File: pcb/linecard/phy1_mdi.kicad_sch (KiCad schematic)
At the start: 51 parts, among them J5 LPJT476156AENL, J9 LPJT476156AENL, U35 VSC8512, U36 ESD224DQAR, U37 ESD224DQAR, U38 ESD224DQAR, U39 ESD224DQAR, U40 ESD224DQAR, U41 ESD224DQAR, U42 ESD224DQAR, U43 ESD224DQAR, U44 ESD224DQAR, U45 ESD224DQAR, U46 ESD224DQAR, U47 ESD224DQAR, U48 ESD224DQAR, U49 ESD224DQAR, U50 ESD224DQAR, U51 ESD224DQAR, U52 ESD224DQAR, U53 ESD224DQAR, U54 ESD224DQAR, U55 ESD224DQAR, U56 ESD224DQAR, U57 ESD224DQAR, U58 ESD224DQAR, U59 ESD224DQAR

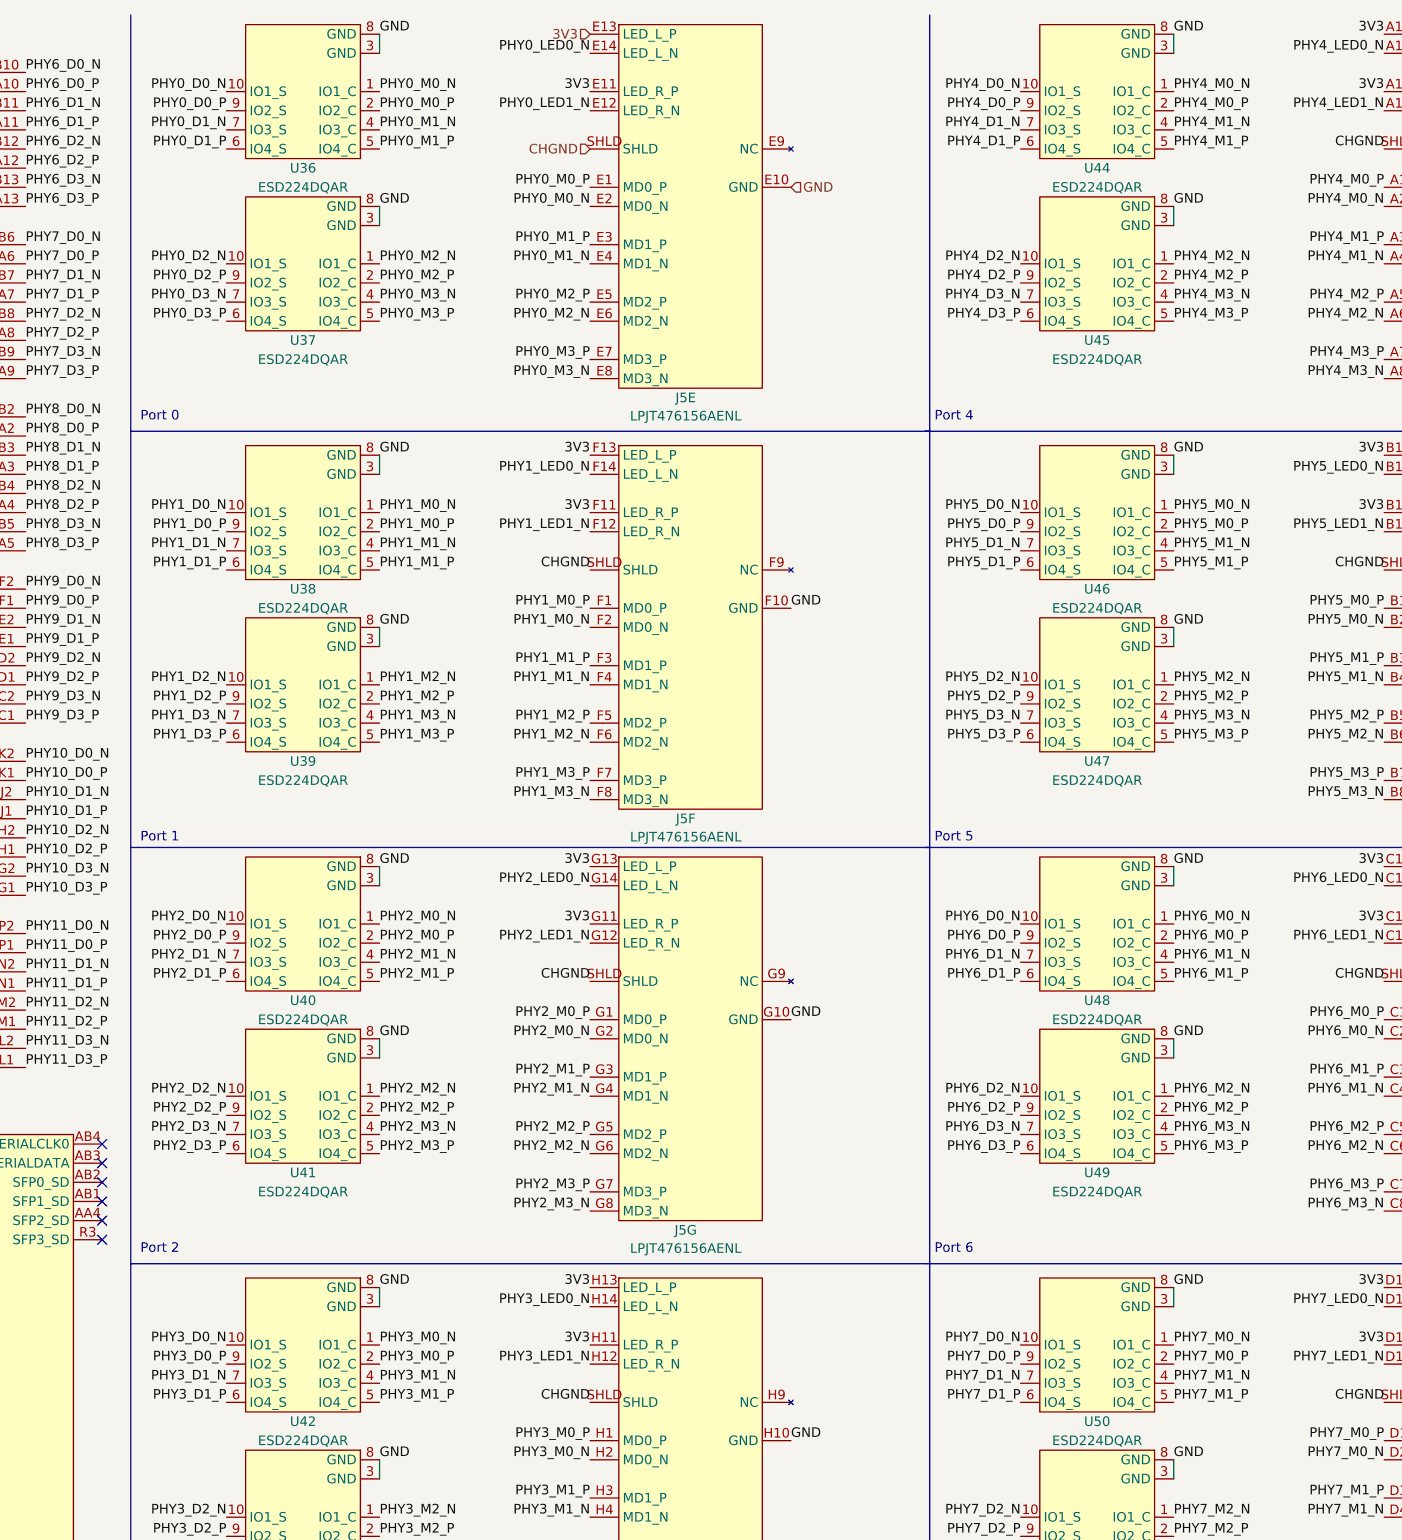
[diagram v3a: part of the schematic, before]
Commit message: Continued routing right VSC8512
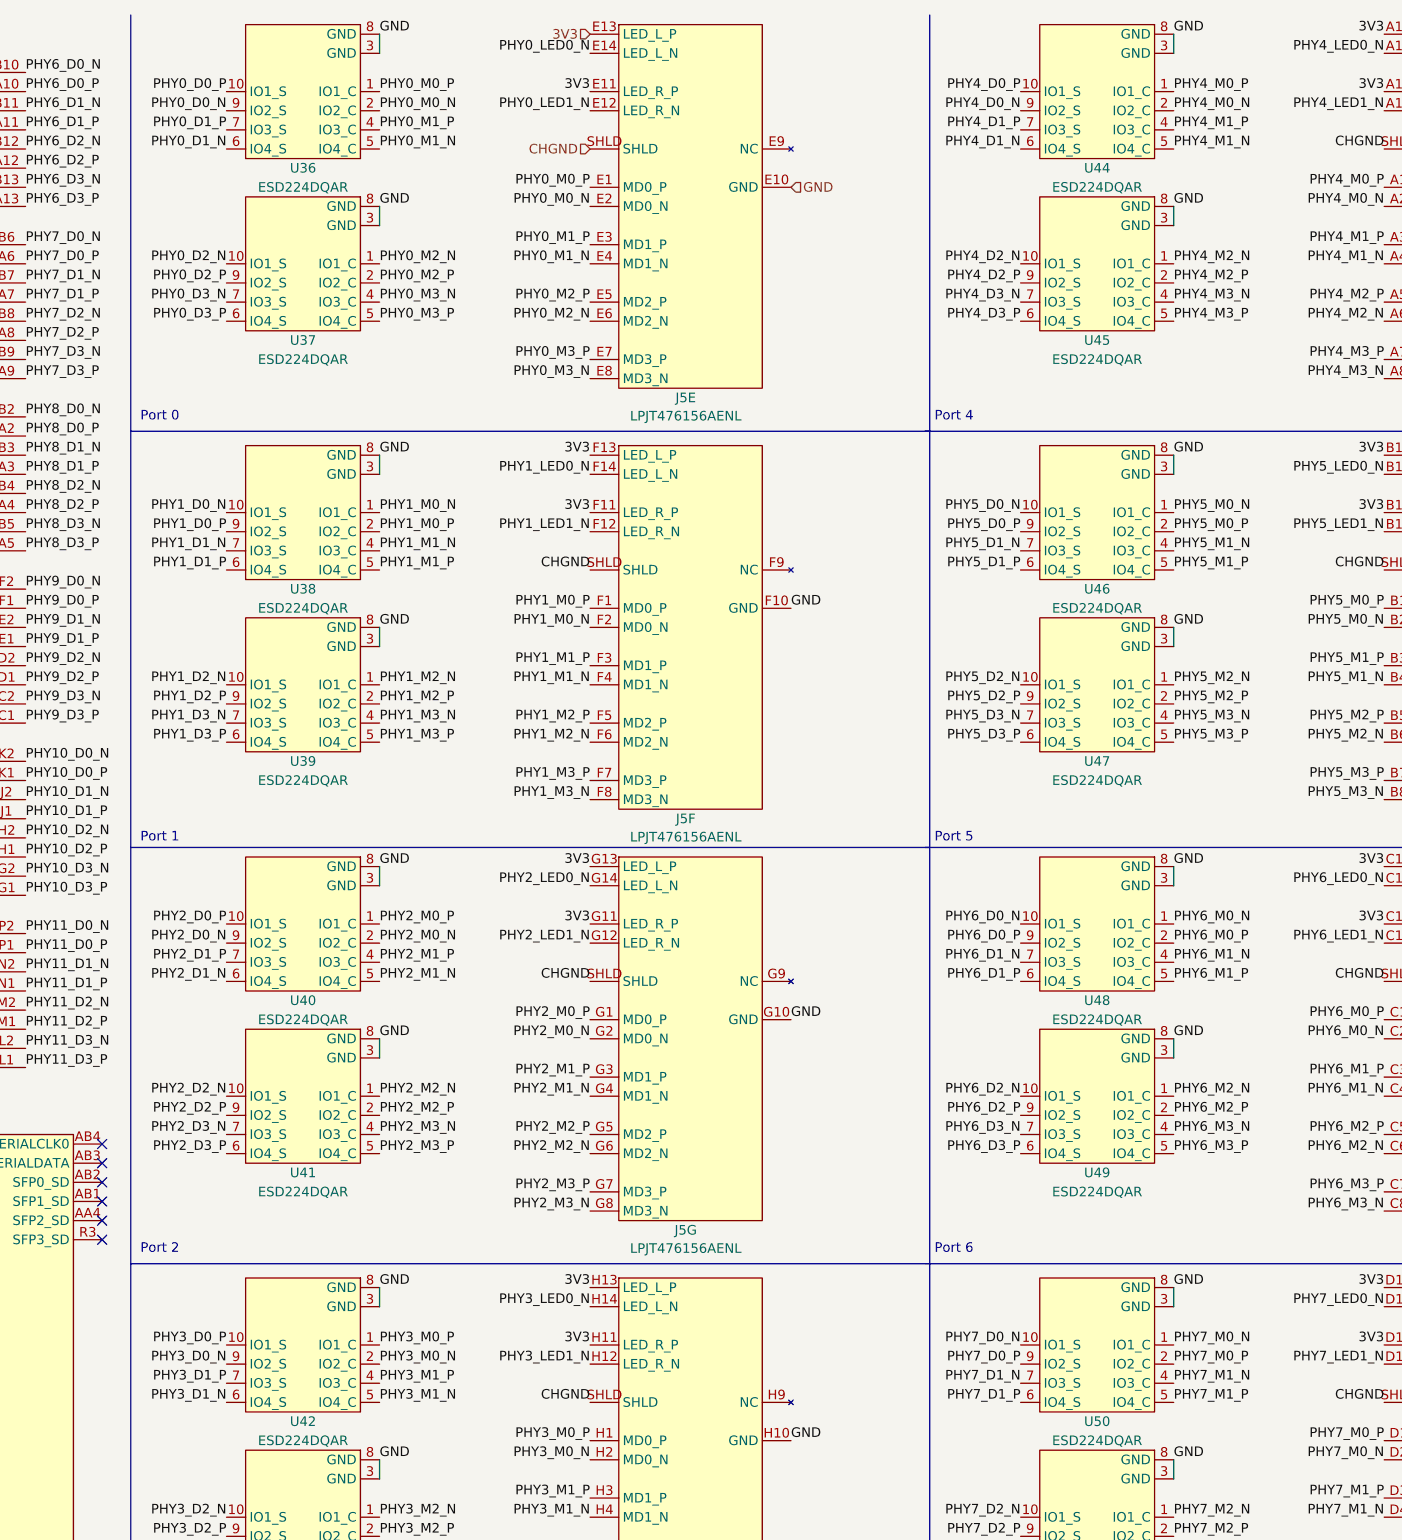
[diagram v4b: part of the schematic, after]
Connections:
- net PHY0_D0_N: now also U36.9 (IO2_S); no longer U36.10 (IO1_S)
- net PHY0_D0_P: now also U36.10 (IO1_S); no longer U36.9 (IO2_S)
- net PHY0_D1_N: now also U36.6 (IO4_S); no longer U36.7 (IO3_S)
- net PHY0_D1_P: now also U36.7 (IO3_S); no longer U36.6 (IO4_S)
- net PHY0_M0_N: now also U36.2 (IO2_C); no longer U36.1 (IO1_C)
- net PHY0_M0_P: now also U36.1 (IO1_C); no longer U36.2 (IO2_C)
- net PHY0_M1_N: now also U36.5 (IO4_C); no longer U36.4 (IO3_C)
- net PHY0_M1_P: now also U36.4 (IO3_C); no longer U36.5 (IO4_C)
- net PHY2_D0_N: now also U40.9 (IO2_S); no longer U40.10 (IO1_S)
- net PHY2_D0_P: now also U40.10 (IO1_S); no longer U40.9 (IO2_S)
- net PHY2_D1_N: now also U40.6 (IO4_S); no longer U40.7 (IO3_S)
- net PHY2_D1_P: now also U40.7 (IO3_S); no longer U40.6 (IO4_S)
- net PHY2_M0_N: now also U40.2 (IO2_C); no longer U40.1 (IO1_C)
- net PHY2_M0_P: now also U40.1 (IO1_C); no longer U40.2 (IO2_C)
- net PHY2_M1_N: now also U40.5 (IO4_C); no longer U40.4 (IO3_C)
- net PHY2_M1_P: now also U40.4 (IO3_C); no longer U40.5 (IO4_C)
- net PHY3_D0_N: now also U42.9 (IO2_S); no longer U42.10 (IO1_S)
- net PHY3_D0_P: now also U42.10 (IO1_S); no longer U42.9 (IO2_S)
- net PHY3_D1_N: now also U42.6 (IO4_S); no longer U42.7 (IO3_S)
- net PHY3_D1_P: now also U42.7 (IO3_S); no longer U42.6 (IO4_S)
- net PHY3_M0_N: now also U42.2 (IO2_C); no longer U42.1 (IO1_C)
- net PHY3_M0_P: now also U42.1 (IO1_C); no longer U42.2 (IO2_C)
- net PHY3_M1_N: now also U42.5 (IO4_C); no longer U42.4 (IO3_C)
- net PHY3_M1_P: now also U42.4 (IO3_C); no longer U42.5 (IO4_C)
- net PHY4_D0_N: now also U44.9 (IO2_S); no longer U44.10 (IO1_S)
- net PHY4_D0_P: now also U44.10 (IO1_S); no longer U44.9 (IO2_S)
- net PHY4_D1_N: now also U44.6 (IO4_S); no longer U44.7 (IO3_S)
- net PHY4_D1_P: now also U44.7 (IO3_S); no longer U44.6 (IO4_S)
- net PHY4_M0_N: now also U44.2 (IO2_C); no longer U44.1 (IO1_C)
- net PHY4_M0_P: now also U44.1 (IO1_C); no longer U44.2 (IO2_C)
- net PHY4_M1_N: now also U44.5 (IO4_C); no longer U44.4 (IO3_C)
- net PHY4_M1_P: now also U44.4 (IO3_C); no longer U44.5 (IO4_C)
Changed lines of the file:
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@@
 	(title_block
 		(title "LATENTRED Line Card")
-		(date "2024-12-14")
+		(date "2024-12-15")
 		(rev "0.1")
 		(company "Antikernel Labs")
@@
 	)
 	(label "PHY3_D0_P"
-		(at 102.87 191.77 180)
+		(at 102.87 189.23 180)
 		(fields_autoplaced yes)
 		(effects
@@
 	)
 	(label "PHY4_D1_P"
-		(at 208.28 30.48 180)
+		(at 208.28 27.94 180)
 		(fields_autoplaced yes)
 		(effects
@@
 	)
 	(label "PHY0_M1_N"
-		(at 123.19 27.94 0)
+		(at 123.19 30.48 0)
 		(fields_autoplaced yes)
 		(effects
@@
 	)
 	(label "PHY3_D0_N"
-		(at 102.87 189.23 180)
+		(at 102.87 191.77 180)
 		(fields_autoplaced yes)
 		(effects
@@
 	)
 	(label "PHY0_M1_P"
-		(at 123.19 30.48 0)
+		(at 123.19 27.94 0)
 		(fields_autoplaced yes)
 		(effects
@@
 	)
 	(label "PHY2_M0_N"
-		(at 123.19 133.35 0)
+		(at 123.19 135.89 0)
 		(fields_autoplaced yes)
 		(effects
@@
 	)
 	(label "PHY4_M1_N"
-		(at 228.6 27.94 0)
+		(at 228.6 30.48 0)
 		(fields_autoplaced yes)
 		(effects
@@
 	)
 	(label "PHY3_D1_P"
-		(at 102.87 196.85 180)
+		(at 102.87 194.31 180)
 		(fields_autoplaced yes)
 		(effects
@@
 	)
 	(label "PHY4_M0_N"
-		(at 228.6 22.86 0)
+		(at 228.6 25.4 0)
 		(fields_autoplaced yes)
 		(effects
@@
 	)
 	(label "PHY4_M0_P"
-		(at 228.6 25.4 0)
+		(at 228.6 22.86 0)
 		(fields_autoplaced yes)
 		(effects
@@
 	)
 	(label "PHY0_D1_P"
-		(at 102.87 30.48 180)
+		(at 102.87 27.94 180)
 		(fields_autoplaced yes)
 		(effects
@@
 	)
 	(label "PHY4_D0_N"
-		(at 208.28 22.86 180)
+		(at 208.28 25.4 180)
 		(fields_autoplaced yes)
 		(effects
@@
 	)
 	(label "PHY2_D0_N"
-		(at 102.87 133.35 180)
+		(at 102.87 135.89 180)
 		(fields_autoplaced yes)
 		(effects
@@
 	)
 	(label "PHY2_D1_N"
-		(at 102.87 138.43 180)
+		(at 102.87 140.97 180)
 		(fields_autoplaced yes)
 		(effects
@@
 	)
 	(label "PHY3_M1_N"
-		(at 123.19 194.31 0)
+		(at 123.19 196.85 0)
 		(fields_autoplaced yes)
 		(effects
@@
 	)
 	(label "PHY2_D1_P"
-		(at 102.87 140.97 180)
+		(at 102.87 138.43 180)
 		(fields_autoplaced yes)
 		(effects
@@
 	)
 	(label "PHY4_D1_N"
-		(at 208.28 27.94 180)
+		(at 208.28 30.48 180)
 		(fields_autoplaced yes)
 		(effects
@@
 	)
 	(label "PHY3_M1_P"
-		(at 123.19 196.85 0)
+		(at 123.19 194.31 0)
 		(fields_autoplaced yes)
 		(effects
@@
 	)
 	(label "PHY2_D0_P"
-		(at 102.87 135.89 180)
+		(at 102.87 133.35 180)
 		(fields_autoplaced yes)
 		(effects
@@
 	)
 	(label "PHY3_M0_P"
-		(at 123.19 191.77 0)
+		(at 123.19 189.23 0)
 		(fields_autoplaced yes)
 		(effects
@@
 	)
 	(label "PHY4_M1_P"
-		(at 228.6 30.48 0)
+		(at 228.6 27.94 0)
 		(fields_autoplaced yes)
 		(effects
@@
 	)
 	(label "PHY0_M0_P"
-		(at 123.19 25.4 0)
+		(at 123.19 22.86 0)
 		(fields_autoplaced yes)
 		(effects
@@
 	)
 	(label "PHY2_M1_P"
-		(at 123.19 140.97 0)
+		(at 123.19 138.43 0)
 		(fields_autoplaced yes)
 		(effects
@@
 	)
 	(label "PHY2_M0_P"
-		(at 123.19 135.89 0)
+		(at 123.19 133.35 0)
 		(fields_autoplaced yes)
 		(effects
@@
 	)
 	(label "PHY0_D1_N"
-		(at 102.87 27.94 180)
+		(at 102.87 30.48 180)
 		(fields_autoplaced yes)
 		(effects
@@
 	)
 	(label "PHY2_M1_N"
-		(at 123.19 138.43 0)
+		(at 123.19 140.97 0)
 		(fields_autoplaced yes)
 		(effects
@@
 	)
 	(label "PHY0_D0_P"
-		(at 102.87 25.4 180)
+		(at 102.87 22.86 180)
 		(fields_autoplaced yes)
 		(effects
@@
 	)
 	(label "PHY3_M0_N"
-		(at 123.19 189.23 0)
+		(at 123.19 191.77 0)
 		(fields_autoplaced yes)
 		(effects
@@
 	)
 	(label "PHY0_D0_N"
-		(at 102.87 22.86 180)
+		(at 102.87 25.4 180)
 		(fields_autoplaced yes)
 		(effects
@@
 	)
 	(label "PHY4_D0_P"
-		(at 208.28 25.4 180)
+		(at 208.28 22.86 180)
 		(fields_autoplaced yes)
 		(effects
@@
 	)
 	(label "PHY3_D1_N"
-		(at 102.87 194.31 180)
+		(at 102.87 196.85 180)
 		(fields_autoplaced yes)
 		(effects
@@
 	)
 	(label "PHY0_M0_N"
-		(at 123.19 22.86 0)
+		(at 123.19 25.4 0)
 		(fields_autoplaced yes)
 		(effects
